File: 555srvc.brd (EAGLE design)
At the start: 19.6 x 6.9 mm, 10 parts, among them IC1 555

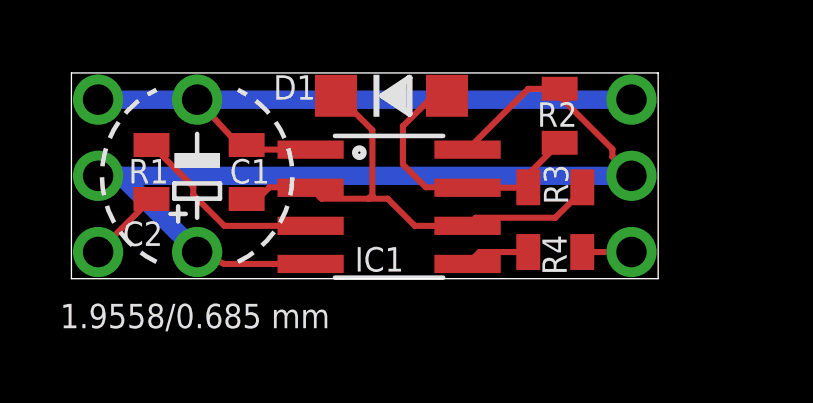
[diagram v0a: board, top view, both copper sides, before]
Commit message: added symbols for in/out and updated lib for capacitor pakcge
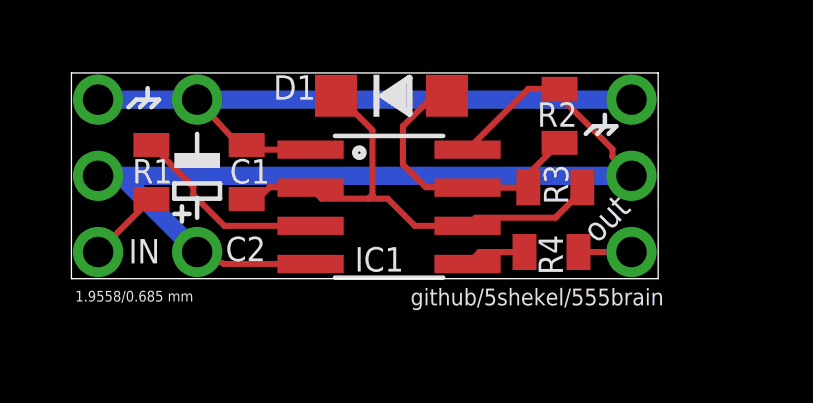
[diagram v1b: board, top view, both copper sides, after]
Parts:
- moved R4 0.13 mm to (16.0, 0.89)
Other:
- board text added: "IN"
- board text added: "github/5shekel/555brain"
- board text added: "out"
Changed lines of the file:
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@@
 <setting verticaltext="up"/>
 </settings>
-<grid distance="5" unitdist="mil" unit="mil" style="lines" multiple="1" display="no" altdistance="50" altunitdist="mil" altunit="mil"/>
+<grid distance="5" unitdist="mil" unit="mil" style="lines" multiple="1" display="yes" altdistance="50" altunitdist="mil" altunit="mil"/>
 <layers>
 <layer number="1" name="Top" color="4" fill="1" visible="yes" active="yes"/>
@@
 <layer number="99" name="SpiceOrder" color="7" fill="1" visible="no" active="no"/>
 <layer number="100" name="Muster" color="7" fill="1" visible="no" active="no"/>
-<layer number="101" name="Patch_Top" color="12" fill="4" visible="yes" active="yes"/>
+<layer number="101" name="Patch_Top" color="7" fill="1" visible="yes" active="yes"/>
 <layer number="102" name="Vscore" color="7" fill="1" visible="yes" active="yes"/>
-<layer number="103" name="fp3" color="7" fill="1" visible="no" active="yes"/>
+<layer number="103" name="fp3" color="7" fill="1" visible="yes" active="yes"/>
 <layer number="104" name="Name" color="7" fill="1" visible="yes" active="yes"/>
-<layer number="105" name="Beschreib" color="9" fill="1" visible="yes" active="yes"/>
-<layer number="106" name="BGA-Top" color="4" fill="1" visible="yes" active="yes"/>
-<layer number="107" name="BD-Top" color="5" fill="1" visible="yes" active="yes"/>
-<layer number="108" name="fp8" color="7" fill="1" visible="no" active="yes"/>
-<layer number="109" name="fp9" color="7" fill="1" visible="no" active="yes"/>
-<layer number="110" name="fp0" color="7" fill="1" visible="no" active="yes"/>
+<layer number="105" name="Beschreib" color="7" fill="1" visible="yes" active="yes"/>
+<layer number="106" name="BGA-Top" color="7" fill="1" visible="yes" active="yes"/>
+<layer number="107" name="BD-Top" color="7" fill="1" visible="yes" active="yes"/>
+<layer number="108" name="fp8" color="7" fill="1" visible="yes" active="yes"/>
+<layer number="109" name="fp9" color="7" fill="1" visible="yes" active="yes"/>
+<layer number="110" name="fp0" color="7" fill="1" visible="yes" active="yes"/>
 <layer number="111" name="LPC17xx" color="7" fill="1" visible="yes" active="yes"/>
 <layer number="112" name="tSilk" color="7" fill="1" visible="yes" active="yes"/>
 <layer number="113" name="IDFDebug" color="7" fill="1" visible="yes" active="yes"/>
-<layer number="116" name="Patch_BOT" color="9" fill="4" visible="yes" active="yes"/>
+<layer number="116" name="Patch_BOT" color="7" fill="1" visible="yes" active="yes"/>
 <layer number="118" name="Rect_Pads" color="7" fill="1" visible="no" active="no"/>
 <layer number="121" name="_tsilk" color="7" fill="1" visible="yes" active="yes"/>
 <layer number="122" name="_bsilk" color="7" fill="1" visible="yes" active="yes"/>
-<layer number="123" name="tTestmark" color="7" fill="1" visible="no" active="yes"/>
-<layer number="124" name="bTestmark" color="7" fill="1" visible="no" active="yes"/>
+<layer number="123" name="tTestmark" color="7" fill="1" visible="yes" active="yes"/>
+<layer number="124" name="bTestmark" color="7" fill="1" visible="yes" active="yes"/>
 <layer number="125" name="_tNames" color="7" fill="1" visible="yes" active="yes"/>
 <layer number="126" name="_bNames" color="7" fill="1" visible="yes" active="yes"/>
 <layer number="127" name="_tValues" color="7" fill="1" visible="yes" active="yes"/>
 <layer number="128" name="_bValues" color="7" fill="1" visible="yes" active="yes"/>
-<layer number="131" name="tAdjust" color="7" fill="1" visible="no" active="yes"/>
-<layer number="132" name="bAdjust" color="7" fill="1" visible="no" active="yes"/>
+<layer number="131" name="tAdjust" color="7" fill="1" visible="yes" active="yes"/>
+<layer number="132" name="bAdjust" color="7" fill="1" visible="yes" active="yes"/>
 <layer number="144" name="Drill_legend" color="7" fill="1" visible="yes" active="yes"/>
 <layer number="150" name="Notes" color="7" fill="1" visible="yes" active="yes"/>
@@
 <layer number="155" name="FabDoc3" color="7" fill="1" visible="yes" active="yes"/>
 <layer number="199" name="Contour" color="7" fill="1" visible="yes" active="yes"/>
-<layer number="200" name="200bmp" color="1" fill="10" visible="yes" active="yes"/>
+<layer number="200" name="200bmp" color="7" fill="1" visible="yes" active="yes"/>
 <layer number="201" name="201bmp" color="2" fill="1" visible="no" active="no"/>
 <layer number="202" name="202bmp" color="3" fill="1" visible="no" active="no"/>
-<layer number="203" name="203bmp" color="4" fill="10" visible="yes" active="yes"/>
-<layer number="204" name="204bmp" color="5" fill="10" visible="yes" active="yes"/>
-<layer number="205" name="205bmp" color="6" fill="10" visible="yes" active="yes"/>
-<layer number="206" name="206bmp" color="7" fill="10" visible="yes" active="yes"/>
-<layer number="207" name="207bmp" color="8" fill="10" visible="yes" active="yes"/>
-<layer number="208" name="208bmp" color="9" fill="10" visible="yes" active="yes"/>
-<layer number="209" name="209bmp" color="7" fill="1" visible="no" active="yes"/>
-<layer number="210" name="210bmp" color="7" fill="1" visible="no" active="yes"/>
+<layer number="203" name="203bmp" color="7" fill="1" visible="yes" active="yes"/>
+<layer number="204" name="204bmp" color="7" fill="1" visible="yes" active="yes"/>
+<layer number="205" name="205bmp" color="7" fill="1" visible="yes" active="yes"/>
+<layer number="206" name="206bmp" color="7" fill="1" visible="yes" active="yes"/>
+<layer number="207" name="207bmp" color="7" fill="1" visible="yes" active="yes"/>
+<layer number="208" name="208bmp" color="7" fill="1" visible="yes" active="yes"/>
+<layer number="209" name="209bmp" color="7" fill="1" visible="yes" active="yes"/>
+<layer number="210" name="210bmp" color="7" fill="1" visible="yes" active="yes"/>
 <layer number="211" name="211bmp" color="7" fill="1" visible="yes" active="yes"/>
 <layer number="212" name="212bmp" color="7" fill="1" visible="yes" active="yes"/>
@@
 <wire x1="19.558" y1="6.858" x2="0" y2="6.858" width="0" layer="20"/>
 <wire x1="0" y1="6.858" x2="0" y2="0" width="0" layer="20"/>
-<text x="-0.381" y="-1.651" size="0.8128" layer="21">1.9558/0.685 mm</text>
+<text x="0.127" y="-0.762" size="0.3556" layer="21">1.9558/0.685 mm</text>
+<text x="11.303" y="-0.889" size="0.5588" layer="21">github/5shekel/555brain</text>
+<wire x1="17.78" y1="5.08" x2="17.526" y2="4.826" width="0.1524" layer="21"/>
+<wire x1="18.161" y1="5.08" x2="17.907" y2="4.826" width="0.1524" layer="21"/>
+<wire x1="17.145" y1="4.826" x2="17.399" y2="5.08" width="0.1524" layer="21"/>
+<wire x1="17.399" y1="5.08" x2="17.78" y2="5.08" width="0.1524" layer="21"/>
+<wire x1="17.78" y1="5.08" x2="18.161" y2="5.08" width="0.1524" layer="21"/>
+<wire x1="17.78" y1="5.08" x2="17.78" y2="5.461" width="0.1524" layer="21"/>
+<text x="1.905" y="0.508" size="0.8128" layer="21">IN</text>
+<text x="17.526" y="1.143" size="0.8128" layer="21" rot="R45">out</text>
+<wire x1="2.54" y1="5.969" x2="2.286" y2="5.715" width="0.1524" layer="21"/>
+<wire x1="2.921" y1="5.969" x2="2.667" y2="5.715" width="0.1524" layer="21"/>
+<wire x1="1.905" y1="5.715" x2="2.159" y2="5.969" width="0.1524" layer="21"/>
+<wire x1="2.159" y1="5.969" x2="2.54" y2="5.969" width="0.1524" layer="21"/>
+<wire x1="2.54" y1="5.969" x2="2.921" y2="5.969" width="0.1524" layer="21"/>
+<wire x1="2.54" y1="5.969" x2="2.54" y2="6.35" width="0.1524" layer="21"/>
 </plain>
 <attributes>
@@
 </element>
 <element name="R1" library="555srvc" package="0805" value="2.2k" x="2.667" y="3.556" smashed="yes" rot="R270">
-<attribute name="NAME" x="1.905" y="3.175" size="0.8128" layer="25"/>
+<attribute name="NAME" x="2.032" y="3.175" size="0.8128" layer="25"/>
 <attribute name="VALUE" x="1.27" y="8.382" size="0.8128" layer="27" rot="R270"/>
 </element>
@@
 <attribute name="VALUE" x="19.177" y="5.08" size="0.8128" layer="27" rot="R180"/>
 </element>
-<element name="R4" library="555srvc" package="0805" value="15k" x="16.129" y="0.889" smashed="yes">
-<attribute name="NAME" x="16.51" y="0.127" size="0.8128" layer="25" rot="R90"/>
-<attribute name="VALUE" x="13.462" y="1.905" size="0.8128" layer="27"/>
+<element name="R4" library="555srvc" package="0805" value="15k" x="16.002" y="0.889" smashed="yes">
+<attribute name="NAME" x="16.383" y="0.127" size="0.8128" layer="25" rot="R90"/>
+<attribute name="VALUE" x="13.335" y="1.905" size="0.8128" layer="27"/>
 </element>
 <element name="C2" library="555srvc" package="E5-6" value="" x="4.191" y="3.429" smashed="yes" rot="R90">
-<attribute name="NAME" x="3.048" y="1.905" size="0.8128" layer="25" ratio="10" rot="R180"/>
+<attribute name="NAME" x="6.477" y="1.397" size="0.8128" layer="25" ratio="10" rot="R180"/>
 <attribute name="VALUE" x="7.112" y="6.477" size="1.27" layer="27" ratio="10" rot="R90"/>
 </element>
@@
 <contactref element="IC1" pad="5"/>
 <contactref element="R4" pad="1"/>
-<wire x1="15.229" y1="0.889" x2="13.6012" y2="0.889" width="0.2032" layer="1"/>
+<wire x1="15.102" y1="0.889" x2="13.6012" y2="0.889" width="0.2032" layer="1"/>
 <wire x1="13.6012" y1="0.889" x2="13.2042" y2="0.492" width="0.2032" layer="1"/>
 </signal>
@@
 <contactref element="R4" pad="2"/>
 <contactref element="JP3" pad="3"/>
-<wire x1="18.669" y1="0.889" x2="17.029" y2="0.889" width="0.2032" layer="1"/>
+<wire x1="18.669" y1="0.889" x2="16.902" y2="0.889" width="0.2032" layer="1"/>
 </signal>
 </signals>

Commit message: update pic, and sorted silkscreen
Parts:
- JP2: value SERVO_OUT -> servo_out
- moved R2 0.76 mm to (15.5, 5.43)
- moved C1 0.13 mm to (5.84, 3.43)
- moved C2 0.13 mm to (4.32, 3.43)
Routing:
- net N$1: track 16.5 -> 15.9 mm
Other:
- board text added: "in"
- board text removed: "IN"

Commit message: new layout
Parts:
- JP2: value servo_out -> SERVO_OUT
- moved R1 2.72 mm to (4.32, 1.40)
- moved JP3 2.54 mm to (21.2, 3.43)
- moved C2 2.41 mm to (6.73, 3.43)
- moved C1 1.98 mm to (4.32, 4.70)
- moved R2 1.83 mm to (17.3, 4.95)
- moved R4 1.66 mm to (17.7, 0.76)
- moved R3 1.65 mm to (17.7, 2.41), turned to 0 degrees
- moved IC1 1.50 mm to (12.1, 2.67)
- moved D1 1.40 mm to (12.1, 6.10)
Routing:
- net GND: track 22.2 -> 25.8 mm
- net VCC: track 33.6 -> 36.9 mm
- net N$1: track 15.9 -> 17.7 mm
- net N$5: track 6.58 -> 5.14 mm
- net SERVO_OUT: track 2.51 -> 3.45 mm
- net INPUT: track 1.77 -> 2.66 mm
- net N$2: track 9.72 -> 10.5 mm
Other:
- board size 19.6 x 6.9 mm -> 22.1 x 6.9 mm
- board text removed: "1.9558/0.685 mm"
- board text removed: "github/5shekel/555brain"
